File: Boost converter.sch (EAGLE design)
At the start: 21 parts, among them IC1 NE555N, IC2 attiny84, IC3 attiny85, Q1 2n7000, Q2 zvp4105

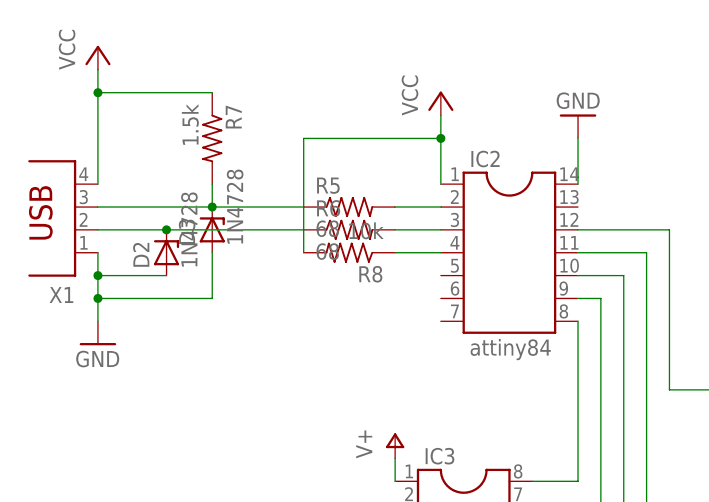
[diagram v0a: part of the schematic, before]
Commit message: Rerouted USB data lines
rerouted usb D- line to pin 6 on the attiny84 socket and D+ line to pin 5(int0) on attiny84 socket. pins 2 and 3 on socket were left unconnected but I still need to add crystal oscillator to board and connect it to these pins
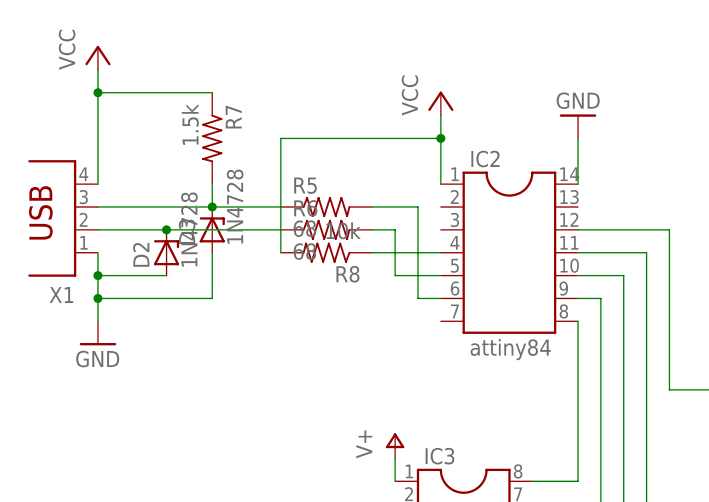
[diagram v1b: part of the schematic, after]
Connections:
- net N$4: now also IC2.6; no longer IC2.2
- net N$5: now also IC2.5; no longer IC2.3
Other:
- moved on the sheet: R5, R6, R8
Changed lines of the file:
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@@
 <instance part="GND7" gate="1" x="-20.32" y="48.26"/>
 <instance part="P+10" gate="1" x="142.24" y="83.82"/>
-<instance part="R5" gate="G$1" x="-25.4" y="91.44"/>
-<instance part="R6" gate="G$1" x="-25.4" y="88.9"/>
+<instance part="R5" gate="G$1" x="-27.94" y="91.44"/>
+<instance part="R6" gate="G$1" x="-27.94" y="88.9"/>
 <instance part="R7" gate="G$1" x="-40.64" y="99.06" rot="R270"/>
 <instance part="D2" gate="1" x="-45.72" y="86.36" rot="R90"/>
@@
 <instance part="P+11" gate="VCC" x="-40.64" y="55.88"/>
 <instance part="GND8" gate="1" x="-40.64" y="35.56"/>
-<instance part="R8" gate="G$1" x="-25.4" y="86.36" rot="R180"/>
+<instance part="R8" gate="G$1" x="-27.94" y="86.36" rot="R180"/>
 <instance part="P+12" gate="1" x="-20.32" y="66.04"/>
 </instances>
@@
 <pinref part="R8" gate="G$1" pin="2"/>
 <wire x1="-15.24" y1="99.06" x2="-15.24" y2="101.6" width="0.1524" layer="91"/>
-<wire x1="-30.48" y1="86.36" x2="-30.48" y2="99.06" width="0.1524" layer="91"/>
-<wire x1="-30.48" y1="99.06" x2="-15.24" y2="99.06" width="0.1524" layer="91"/>
+<wire x1="-33.02" y1="86.36" x2="-33.02" y2="99.06" width="0.1524" layer="91"/>
+<wire x1="-33.02" y1="99.06" x2="-15.24" y2="99.06" width="0.1524" layer="91"/>
 <junction x="-15.24" y="99.06"/>
 </segment>
@@
 <wire x1="-53.34" y1="88.9" x2="-45.72" y2="88.9" width="0.1524" layer="91"/>
 <pinref part="R6" gate="G$1" pin="1"/>
-<wire x1="-30.48" y1="88.9" x2="-45.72" y2="88.9" width="0.1524" layer="91"/>
+<wire x1="-33.02" y1="88.9" x2="-45.72" y2="88.9" width="0.1524" layer="91"/>
 <junction x="-45.72" y="88.9"/>
 </segment>
@@
 <junction x="-40.64" y="91.44"/>
 <pinref part="R5" gate="G$1" pin="1"/>
-<wire x1="-40.64" y1="91.44" x2="-30.48" y2="91.44" width="0.1524" layer="91"/>
-</segment>
-</net>
-<net name="N$4" class="0">
-<segment>
-<pinref part="IC2" gate="G$1" pin="2"/>
-<pinref part="R5" gate="G$1" pin="2"/>
-<wire x1="-15.24" y1="91.44" x2="-20.32" y2="91.44" width="0.1524" layer="91"/>
-</segment>
-</net>
-<net name="N$5" class="0">
-<segment>
-<pinref part="IC2" gate="G$1" pin="3"/>
-<pinref part="R6" gate="G$1" pin="2"/>
-<wire x1="-15.24" y1="88.9" x2="-20.32" y2="88.9" width="0.1524" layer="91"/>
+<wire x1="-40.64" y1="91.44" x2="-33.02" y2="91.44" width="0.1524" layer="91"/>
 </segment>
 </net>
@@
 <pinref part="R8" gate="G$1" pin="1"/>
 <pinref part="IC2" gate="G$1" pin="4"/>
-<wire x1="-20.32" y1="86.36" x2="-15.24" y2="86.36" width="0.1524" layer="91"/>
+<wire x1="-22.86" y1="86.36" x2="-15.24" y2="86.36" width="0.1524" layer="91"/>
 </segment>
 </net>
@@
 </segment>
 </net>
+<net name="N$4" class="0">
+<segment>
+<pinref part="R5" gate="G$1" pin="2"/>
+<wire x1="-22.86" y1="91.44" x2="-17.78" y2="91.44" width="0.1524" layer="91"/>
+<wire x1="-17.78" y1="91.44" x2="-17.78" y2="81.28" width="0.1524" layer="91"/>
+<pinref part="IC2" gate="G$1" pin="6"/>
+<wire x1="-17.78" y1="81.28" x2="-15.24" y2="81.28" width="0.1524" layer="91"/>
+</segment>
+</net>
+<net name="N$5" class="0">
+<segment>
+<pinref part="R6" gate="G$1" pin="2"/>
+<wire x1="-22.86" y1="88.9" x2="-20.32" y2="88.9" width="0.1524" layer="91"/>
+<wire x1="-20.32" y1="88.9" x2="-20.32" y2="83.82" width="0.1524" layer="91"/>
+<pinref part="IC2" gate="G$1" pin="5"/>
+<wire x1="-20.32" y1="83.82" x2="-15.24" y2="83.82" width="0.1524" layer="91"/>
+</segment>
+</net>

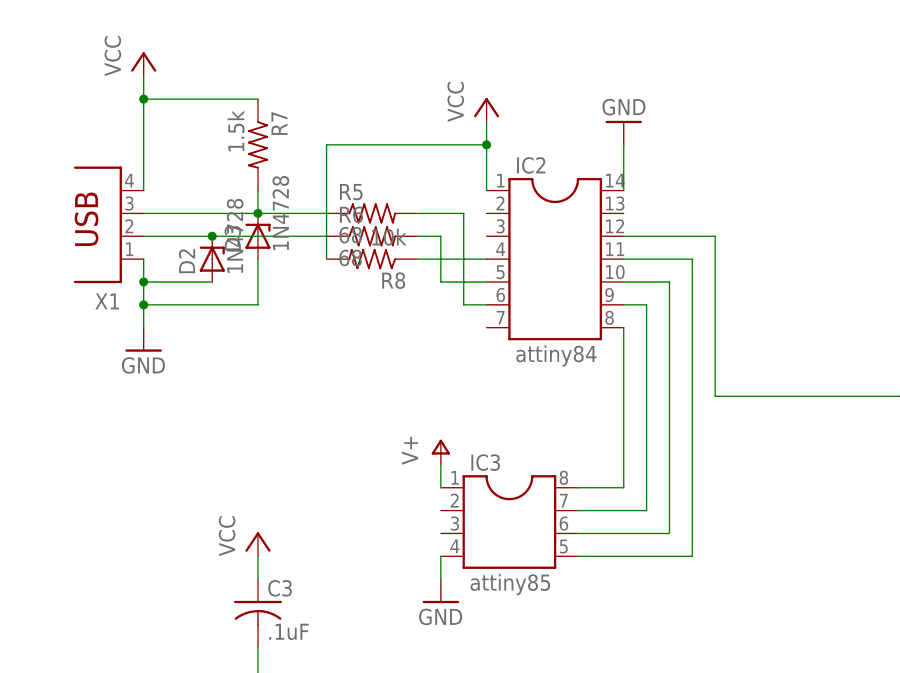
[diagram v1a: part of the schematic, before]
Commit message: Added crystal oscillator
also had to move around boost converter components to make room for the oscillator, not sure how drastic the inductance and capacitance changes from the pcb lines will be and if it will have a large impact on boost converter output voltage. if I do get this new board fabricated and the voltage does change significantly, I can just switch out the converter diode to drop the voltage to the right level. also added line from attiny84 io pin to attiny85 pb3 on pin 2
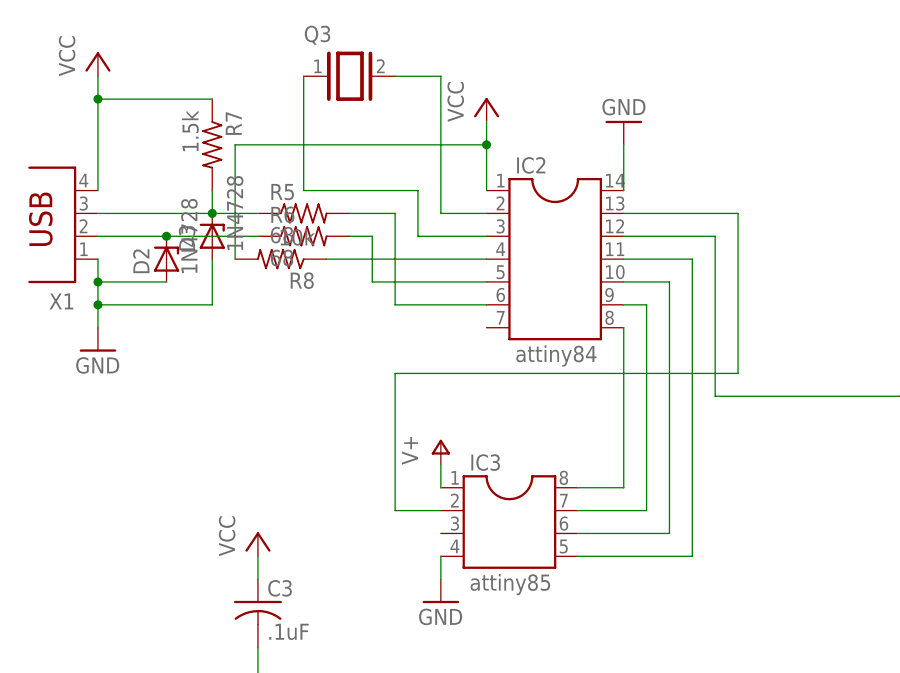
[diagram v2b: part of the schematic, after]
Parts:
- added Q3: (no value), special:XTAL/S
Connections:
- new net N$11: IC2.13, IC3.2
- new net N$16: IC2.3, Q3.1
- new net N$17: IC2.2, Q3.2
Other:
- moved on the sheet: D2, D3, R5, R6, R7, R8, X1
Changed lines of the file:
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@@
 <part name="R8" library="resistor" deviceset="R-US_" device="0204/7" value="10k"/>
 <part name="P+12" library="supply1" deviceset="V+" device=""/>
+<part name="Q3" library="special" deviceset="XTAL/S" device=""/>
 </parts>
 <sheets>
@@
 <instance part="P+6" gate="1" x="55.88" y="93.98"/>
 <instance part="P+5" gate="VCC" x="40.64" y="53.34" rot="R180"/>
-<instance part="X1" gate="G$1" x="-55.88" y="91.44" rot="R180"/>
-<instance part="GND5" gate="1" x="-53.34" y="76.2"/>
-<instance part="P+7" gate="VCC" x="-53.34" y="109.22"/>
+<instance part="X1" gate="G$1" x="-60.96" y="91.44" rot="R180"/>
+<instance part="GND5" gate="1" x="-58.42" y="76.2"/>
+<instance part="P+7" gate="VCC" x="-58.42" y="109.22"/>
 <instance part="IC2" gate="G$1" x="-7.62" y="86.36"/>
 <instance part="GND6" gate="1" x="0" y="101.6" rot="R180"/>
@@
 <instance part="GND7" gate="1" x="-20.32" y="48.26"/>
 <instance part="P+10" gate="1" x="142.24" y="83.82"/>
-<instance part="R5" gate="G$1" x="-27.94" y="91.44"/>
-<instance part="R6" gate="G$1" x="-27.94" y="88.9"/>
-<instance part="R7" gate="G$1" x="-40.64" y="99.06" rot="R270"/>
-<instance part="D2" gate="1" x="-45.72" y="86.36" rot="R90"/>
-<instance part="D3" gate="1" x="-40.64" y="88.9" rot="R90"/>
+<instance part="R5" gate="G$1" x="-35.56" y="91.44"/>
+<instance part="R6" gate="G$1" x="-35.56" y="88.9"/>
+<instance part="R7" gate="G$1" x="-45.72" y="99.06" rot="R270"/>
+<instance part="D2" gate="1" x="-50.8" y="86.36" rot="R90"/>
+<instance part="D3" gate="1" x="-45.72" y="88.9" rot="R90"/>
 <instance part="C3" gate="G$1" x="-40.64" y="48.26"/>
 <instance part="P+11" gate="VCC" x="-40.64" y="55.88"/>
 <instance part="GND8" gate="1" x="-40.64" y="35.56"/>
-<instance part="R8" gate="G$1" x="-27.94" y="86.36" rot="R180"/>
+<instance part="R8" gate="G$1" x="-38.1" y="86.36" rot="R180"/>
 <instance part="P+12" gate="1" x="-20.32" y="66.04"/>
+<instance part="Q3" gate="G$1" x="-30.48" y="106.68"/>
 </instances>
 <busses>
@@
 <pinref part="X1" gate="G$1" pin="1"/>
 <pinref part="GND5" gate="1" pin="GND"/>
-<wire x1="-53.34" y1="86.36" x2="-53.34" y2="83.82" width="0.1524" layer="91"/>
+<wire x1="-58.42" y1="86.36" x2="-58.42" y2="83.82" width="0.1524" layer="91"/>
 <pinref part="D2" gate="1" pin="A"/>
-<wire x1="-53.34" y1="83.82" x2="-53.34" y2="81.28" width="0.1524" layer="91"/>
-<wire x1="-53.34" y1="81.28" x2="-53.34" y2="78.74" width="0.1524" layer="91"/>
-<wire x1="-45.72" y1="83.82" x2="-53.34" y2="83.82" width="0.1524" layer="91"/>
-<junction x="-53.34" y="83.82"/>
+<wire x1="-58.42" y1="83.82" x2="-58.42" y2="81.28" width="0.1524" layer="91"/>
+<wire x1="-58.42" y1="81.28" x2="-58.42" y2="78.74" width="0.1524" layer="91"/>
+<wire x1="-50.8" y1="83.82" x2="-58.42" y2="83.82" width="0.1524" layer="91"/>
+<junction x="-58.42" y="83.82"/>
 <pinref part="D3" gate="1" pin="A"/>
-<wire x1="-40.64" y1="86.36" x2="-40.64" y2="81.28" width="0.1524" layer="91"/>
-<wire x1="-40.64" y1="81.28" x2="-53.34" y2="81.28" width="0.1524" layer="91"/>
-<junction x="-53.34" y="81.28"/>
+<wire x1="-45.72" y1="86.36" x2="-45.72" y2="81.28" width="0.1524" layer="91"/>
+<wire x1="-45.72" y1="81.28" x2="-58.42" y2="81.28" width="0.1524" layer="91"/>
+<junction x="-58.42" y="81.28"/>
 </segment>
 <segment>
@@
 <pinref part="P+7" gate="VCC" pin="VCC"/>
 <pinref part="X1" gate="G$1" pin="4"/>
-<wire x1="-53.34" y1="106.68" x2="-53.34" y2="104.14" width="0.1524" layer="91"/>
+<wire x1="-58.42" y1="106.68" x2="-58.42" y2="104.14" width="0.1524" layer="91"/>
 <pinref part="R7" gate="G$1" pin="1"/>
-<wire x1="-53.34" y1="104.14" x2="-53.34" y2="93.98" width="0.1524" layer="91"/>
-<wire x1="-40.64" y1="104.14" x2="-53.34" y2="104.14" width="0.1524" layer="91"/>
-<junction x="-53.34" y="104.14"/>
+<wire x1="-58.42" y1="104.14" x2="-58.42" y2="93.98" width="0.1524" layer="91"/>
+<wire x1="-45.72" y1="104.14" x2="-58.42" y2="104.14" width="0.1524" layer="91"/>
+<junction x="-58.42" y="104.14"/>
 </segment>
 <segment>
@@
 <pinref part="R8" gate="G$1" pin="2"/>
 <wire x1="-15.24" y1="99.06" x2="-15.24" y2="101.6" width="0.1524" layer="91"/>
-<wire x1="-33.02" y1="86.36" x2="-33.02" y2="99.06" width="0.1524" layer="91"/>
-<wire x1="-33.02" y1="99.06" x2="-15.24" y2="99.06" width="0.1524" layer="91"/>
+<wire x1="-43.18" y1="86.36" x2="-43.18" y2="99.06" width="0.1524" layer="91"/>
+<wire x1="-43.18" y1="99.06" x2="-15.24" y2="99.06" width="0.1524" layer="91"/>
 <junction x="-15.24" y="99.06"/>
 </segment>
@@
 <pinref part="X1" gate="G$1" pin="2"/>
 <pinref part="D2" gate="1" pin="C"/>
-<wire x1="-53.34" y1="88.9" x2="-45.72" y2="88.9" width="0.1524" layer="91"/>
+<wire x1="-58.42" y1="88.9" x2="-50.8" y2="88.9" width="0.1524" layer="91"/>
 <pinref part="R6" gate="G$1" pin="1"/>
-<wire x1="-33.02" y1="88.9" x2="-45.72" y2="88.9" width="0.1524" layer="91"/>
-<junction x="-45.72" y="88.9"/>
+<wire x1="-40.64" y1="88.9" x2="-50.8" y2="88.9" width="0.1524" layer="91"/>
+<junction x="-50.8" y="88.9"/>
 </segment>
 </net>
@@
 <pinref part="X1" gate="G$1" pin="3"/>
 <pinref part="D3" gate="1" pin="C"/>
-<wire x1="-53.34" y1="91.44" x2="-40.64" y2="91.44" width="0.1524" layer="91"/>
+<wire x1="-58.42" y1="91.44" x2="-45.72" y2="91.44" width="0.1524" layer="91"/>
 <pinref part="R7" gate="G$1" pin="2"/>
-<wire x1="-40.64" y1="93.98" x2="-40.64" y2="91.44" width="0.1524" layer="91"/>
-<junction x="-40.64" y="91.44"/>
+<wire x1="-45.72" y1="93.98" x2="-45.72" y2="91.44" width="0.1524" layer="91"/>
+<junction x="-45.72" y="91.44"/>
 <pinref part="R5" gate="G$1" pin="1"/>
-<wire x1="-40.64" y1="91.44" x2="-33.02" y2="91.44" width="0.1524" layer="91"/>
+<wire x1="-45.72" y1="91.44" x2="-40.64" y2="91.44" width="0.1524" layer="91"/>
 </segment>
 </net>
@@
 <pinref part="R8" gate="G$1" pin="1"/>
 <pinref part="IC2" gate="G$1" pin="4"/>
-<wire x1="-22.86" y1="86.36" x2="-15.24" y2="86.36" width="0.1524" layer="91"/>
+<wire x1="-33.02" y1="86.36" x2="-15.24" y2="86.36" width="0.1524" layer="91"/>
 </segment>
 </net>
@@
 <segment>
 <pinref part="R5" gate="G$1" pin="2"/>
-<wire x1="-22.86" y1="91.44" x2="-17.78" y2="91.44" width="0.1524" layer="91"/>
-<wire x1="-17.78" y1="91.44" x2="-17.78" y2="81.28" width="0.1524" layer="91"/>
+<wire x1="-30.48" y1="91.44" x2="-25.4" y2="91.44" width="0.1524" layer="91"/>
+<wire x1="-25.4" y1="91.44" x2="-25.4" y2="81.28" width="0.1524" layer="91"/>
 <pinref part="IC2" gate="G$1" pin="6"/>
-<wire x1="-17.78" y1="81.28" x2="-15.24" y2="81.28" width="0.1524" layer="91"/>
+<wire x1="-25.4" y1="81.28" x2="-15.24" y2="81.28" width="0.1524" layer="91"/>
 </segment>
 </net>
@@
 <segment>
 <pinref part="R6" gate="G$1" pin="2"/>
-<wire x1="-22.86" y1="88.9" x2="-20.32" y2="88.9" width="0.1524" layer="91"/>
-<wire x1="-20.32" y1="88.9" x2="-20.32" y2="83.82" width="0.1524" layer="91"/>
+<wire x1="-30.48" y1="88.9" x2="-27.94" y2="88.9" width="0.1524" layer="91"/>
+<wire x1="-27.94" y1="88.9" x2="-27.94" y2="83.82" width="0.1524" layer="91"/>
 <pinref part="IC2" gate="G$1" pin="5"/>
-<wire x1="-20.32" y1="83.82" x2="-15.24" y2="83.82" width="0.1524" layer="91"/>
-</segment>
-</net>
+<wire x1="-27.94" y1="83.82" x2="-15.24" y2="83.82" width="0.1524" layer="91"/>
+</segment>
+</net>
+<net name="N$11" class="0">
+<segment>
+<pinref part="IC2" gate="G$1" pin="13"/>
+<wire x1="0" y1="91.44" x2="12.7" y2="91.44" width="0.1524" layer="91"/>
+<wire x1="12.7" y1="91.44" x2="12.7" y2="73.66" width="0.1524" layer="91"/>
+<wire x1="12.7" y1="73.66" x2="-25.4" y2="73.66" width="0.1524" layer="91"/>
+<wire x1="-25.4" y1="73.66" x2="-25.4" y2="58.42" width="0.1524" layer="91"/>
+<pinref part="IC3" gate="G$1" pin="2"/>
+<wire x1="-25.4" y1="58.42" x2="-20.32" y2="58.42" width="0.1524" layer="91"/>
+</segment>
+</net>
+<net name="N$16" class="0">
+<segment>
+<pinref part="Q3" gate="G$1" pin="1"/>
+<wire x1="-35.56" y1="106.68" x2="-35.56" y2="93.98" width="0.1524" layer="91"/>
+<wire x1="-35.56" y1="93.98" x2="-22.86" y2="93.98" width="0.1524" layer="91"/>
+<wire x1="-22.86" y1="93.98" x2="-22.86" y2="88.9" width="0.1524" layer="91"/>
+<pinref part="IC2" gate="G$1" pin="3"/>
+<wire x1="-22.86" y1="88.9" x2="-15.24" y2="88.9" width="0.1524" layer="91"/>
+</segment>
+</net>
+<net name="N$17" class="0">
+<segment>
+<pinref part="Q3" gate="G$1" pin="2"/>
+<wire x1="-25.4" y1="106.68" x2="-20.32" y2="106.68" width="0.1524" layer="91"/>
+<wire x1="-20.32" y1="106.68" x2="-20.32" y2="91.44" width="0.1524" layer="91"/>
+<pinref part="IC2" gate="G$1" pin="2"/>
+<wire x1="-20.32" y1="91.44" x2="-15.24" y2="91.44" width="0.1524" layer="91"/>
+</segment>
+</net>
